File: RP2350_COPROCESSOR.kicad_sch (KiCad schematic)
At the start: 31 parts, among them J2 Conn_01x05, SW6 SW_Push, SW7 SW_Push, U2 RP2350A, U26 W25Q128JVSIQ, Y6 ABM8-272-T3_12MHZ

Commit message: Finished Last sheets
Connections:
- net CAN_STBY: now reaches U2.14 (GPIO10)
- net USBC_CC1_SENSE: now reaches U2.40 (GPIO26/ADC0)
- net USBC_CC2_SENSE: now reaches U2.41 (GPIO27/ADC1)
- net LF_COIL_A renamed LF_TXCT
- net LF_COIL_B renamed LF_COIL_SEL
- net LF_DEMOD renamed LF_SCIO
- no-connect marks 11 -> 8
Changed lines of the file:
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@@
-	)
-	(no_connect
-		(at 157.48 87.63)
 	)
 	(no_connect
@@
 	)
 	(no_connect
-		(at 157.48 130.81)
-	)
-	(no_connect
 		(at 157.48 90.17)
 	)
@@
 	)
 	(no_connect
-		(at 157.48 133.35)
-	)
-	(no_connect
 		(at 157.48 135.89)
 	)
@@
 	(wire
 		(pts
+			(xy 157.48 133.35) (xy 163.83 133.35)
+		)
+		(stroke
+			(width 0)
+			(type default)
+		)
+	)
+	(wire
+		(pts
 			(xy 93.98 125.73) (xy 106.68 125.73)
 		)
@@
 	(wire
 		(pts
+			(xy 157.48 130.81) (xy 163.83 130.81)
+		)
+		(stroke
+			(width 0)
+			(type default)
+		)
+	)
+	(wire
+		(pts
 			(xy 246.38 59.69) (xy 257.81 59.69)
 		)
@@
 		(pts
 			(xy 168.91 48.26) (xy 168.91 49.53)
+		)
+		(stroke
+			(width 0)
+			(type default)
+		)
+	)
+	(wire
+		(pts
+			(xy 157.48 87.63) (xy 163.83 87.63)
 		)
 		(stroke
@@
 		)
 	)
+	(hierarchical_label "USBC_CC1_SENSE"
+		(shape input)
+		(at 163.83 130.81 0)
+		(effects
+			(font
+				(size 1.27 1.27)
+			)
+			(justify left)
+		)
+	)
 	(hierarchical_label "CC1101_C_GDO0"
 		(shape input)
@@
 		)
 	)
-	(hierarchical_label "LF_DEMOD"
+	(hierarchical_label "LF_SCIO"
 		(shape input)
 		(at 163.83 118.11 0)
@@
 		)
 	)
-	(hierarchical_label "LF_COIL_B"
+	(hierarchical_label "LF_COIL_SEL"
 		(shape output)
 		(at 163.83 115.57 0)
@@
 		)
 	)
-	(hierarchical_label "LF_COIL_A"
+	(hierarchical_label "LF_TXCT"
 		(shape output)
 		(at 163.83 113.03 0)
@@
 		)
 	)
+	(hierarchical_label "CAN_STBY"
+		(shape output)
+		(at 163.83 87.63 0)
+		(effects
+			(font
+				(size 1.27 1.27)
+			)
+			(justify left)
+		)
+	)
 	(hierarchical_label "CC1101_A_GDO0"
 		(shape input)
@@
 		(effects
 			(font
+				(size 1.27 1.27)
+			)
+			(justify left)
+		)
+	)
+	(hierarchical_label "USBC_CC2_SENSE"
+		(shape input)
+		(at 163.83 133.35 0)
+		(effects
+			(font

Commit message: finished annotation
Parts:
- renumbered C28 to C27, C30 to C28, C27 to C29, C29 to C30, C40 to C31, C25 to C32, C31 to C33, C32 to C34, C33 to C35, C34 to C36, C35 to C37, C36 to C38, C37 to C39, C38 to C40, C39 to C41, R23 to R24, R24 to R25, R29 to R26, R30 to R27, R25 to R28, R28 to R29, R27 to R30, R26 to R31
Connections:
- net NFC_DWL_REQ: now reaches U2.27 (GPIO16)
- net NFC_VEN: now reaches U2.28 (GPIO17)
- no-connect marks 8 -> 6
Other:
- title: (none) -> RP2350 Coprocessor, Flash, Debug and USB Host
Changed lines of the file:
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@@
 	(generator_version "10.0")
 	(paper "A4")
+	(title_block
+		(title "RP2350 Coprocessor, Flash, Debug and USB Host")
+		(rev "A")
+	)
 	(text "+3V3 I/O DECOUPLING"
 		(exclude_from_sim no)
@@
 	)
 	(no_connect
-		(at 157.48 102.87)
-	)
-	(no_connect
 		(at 157.48 69.85)
 	)
@@
 	)
 	(no_connect
-		(at 157.48 105.41)
-	)
-	(no_connect
 		(at 157.48 110.49)
 	)
@@
 	(wire
 		(pts
+			(xy 157.48 105.41) (xy 163.83 105.41)
+		)
+		(stroke
+			(width 0)
+			(type default)
+		)
+	)
+	(wire
+		(pts
 			(xy 240.03 115.57) (xy 240.03 107.95)
 		)
@@
 	(wire
 		(pts
+			(xy 157.48 102.87) (xy 163.83 102.87)
+		)
+		(stroke
+			(width 0)
+			(type default)
+		)
+	)
+	(wire
+		(pts
 			(xy 195.58 48.26) (xy 195.58 49.53)
 		)
@@
 		)
 	)
+	(hierarchical_label "NFC_VEN"
+		(shape output)
+		(at 163.83 105.41 0)
+		(effects
+			(font
+				(size 1.27 1.27)
+			)
+			(justify left)
+		)
+	)
 	(hierarchical_label "NFC_SCK"
 		(shape output)
@@
 		)
 	)
+	(hierarchical_label "NFC_DWL_REQ"
+		(shape output)
+		(at 163.83 102.87 0)
+		(effects
+			(font
+				(size 1.27 1.27)
+			)
+			(justify left)
+		)
+	)
 	(hierarchical_label "CC1101_C_GDO0"
 		(shape input)
@@
 		(dnp no)
 		(fields_autoplaced yes)
-		(property "Reference" "C38"
+		(property "Reference" "C40"
 			(at 274.32 52.0699 0)
 			(show_name no)
@@
 			(project "FOBtool_HW"
 				(path "/4178b7d0-cf29-4cf2-b214-acbbbd97d338/27b7c62f-0663-47bb-bbed-fbdc5a64ed05"
-					(reference "C38")
+					(reference "C40")
 					(unit 1)
 				)
@@
 		(in_pos_files yes)
 		(dnp no)
-		(property "Reference" "R29"
+		(property "Reference" "R26"
 			(at 70.104 77.216 90)
 			(show_name no)
@@
 			(project "FOBtool_HW"
 				(path "/4178b7d0-cf29-4cf2-b214-acbbbd97d338/27b7c62f-0663-47bb-bbed-fbdc5a64ed05"
-					(reference "R29")
+					(reference "R26")
 					(unit 1)
 				)
@@
 		(dnp no)
 		(fields_autoplaced yes)
-		(property "Reference" "C33"
+		(property "Reference" "C35"
 			(at 212.09 52.0699 0)
 			(show_name no)
@@
 			(project "FOBtool_HW"
 				(path "/4178b7d0-cf29-4cf2-b214-acbbbd97d338/27b7c62f-0663-47bb-bbed-fbdc5a64ed05"
-					(reference "C33")
+					(reference "C35")
 					(unit 1)
 				)
@@
 		(in_pos_files yes)
 		(dnp no)
-		(property "Reference" "C40"
+		(property "Reference" "C31"
 			(at 35.814 129.032 90)
 			(show_name no)
@@
 			(project "FOBtool_HW"
 				(path "/4178b7d0-cf29-4cf2-b214-acbbbd97d338/27b7c62f-0663-47bb-bbed-fbdc5a64ed05"
-					(reference "C40")
+					(reference "C31")
 					(unit 1)
 				)
@@
 		(dnp no)
 		(fields_autoplaced yes)
-		(property "Reference" "C27"
+		(property "Reference" "C29"
 			(at 186.69 24.1299 0)
 			(show_name no)
@@
 			(project "FOBtool_HW"
 				(path "/4178b7d0-cf29-4cf2-b214-acbbbd97d338/27b7c62f-0663-47bb-bbed-fbdc5a64ed05"
-					(reference "C27")
+					(reference "C29")
 					(unit 1)
 				)
@@
 		(dnp no)
 		(fields_autoplaced yes)
-		(property "Reference" "C30"
+		(property "Reference" "C28"
 			(at 172.72 24.1299 0)
 			(show_name no)
@@
 			(project "FOBtool_HW"
 				(path "/4178b7d0-cf29-4cf2-b214-acbbbd97d338/27b7c62f-0663-47bb-bbed-fbdc5a64ed05"
-					(reference "C30")
+					(reference "C28")
 					(unit 1)
 				)
@@
 		(dnp no)
 		(fields_autoplaced yes)
-		(property "Reference" "C32"
+		(property "Reference" "C34"
 			(at 199.39 52.0699 0)
 			(show_name no)
@@
 			(project "FOBtool_HW"
 				(path "/4178b7d0-cf29-4cf2-b214-acbbbd97d338/27b7c62f-0663-47bb-bbed-fbdc5a64ed05"
-					(reference "C32")
+					(reference "C34")
 					(unit 1)
 				)
@@
 		(in_pos_files yes)
 		(dnp no)
-		(property "Reference" "C29"
+		(property "Reference" "C30"
 			(at 35.814 118.872 90)
 			(show_name no)
@@
 			(project "FOBtool_HW"
 				(path "/4178b7d0-cf29-4cf2-b214-acbbbd97d338/27b7c62f-0663-47bb-bbed-fbdc5a64ed05"
-					(reference "C29")
+					(reference "C30")
 					(unit 1)
 				)
@@
 		(dnp no)
 		(fields_autoplaced yes)
-		(property "Reference" "R24"
+		(property "Reference" "R25"
 			(at 44.45 68.58 90)
 			(show_name no)
@@
 			(project "FOBtool_HW"
 				(path "/4178b7d0-cf29-4cf2-b214-acbbbd97d338/27b7c62f-0663-47bb-bbed-fbdc5a64ed05"
-					(reference "R24")
+					(reference "R25")
 					(unit 1)
 				)
@@
 		(dnp no)
 		(fields_autoplaced yes)
-		(property "Reference" "C25"
+		(property "Reference" "C32"
 			(at 172.72 52.0699 0)
 			(show_name no)
@@
 			(project "FOBtool_HW"
 				(path "/4178b7d0-cf29-4cf2-b214-acbbbd97d338/27b7c62f-0663-47bb-bbed-fbdc5a64ed05"
-					(reference "C25")
+					(reference "C32")
 					(unit 1)
 				)
@@
 		(dnp no)
 		(fields_autoplaced yes)
-		(property "Reference" "C28"
+		(property "Reference" "C27"
 			(at 157.48 24.1299 0)
 			(show_name no)
@@
 			(project "FOBtool_HW"
 				(path "/4178b7d0-cf29-4cf2-b214-acbbbd97d338/27b7c62f-0663-47bb-bbed-fbdc5a64ed05"
-					(reference "C28")
+					(reference "C27")
 					(unit 1)
 				)
@@
 		(dnp no)
 		(fields_autoplaced yes)
-		(property "Reference" "R28"
+		(property "Reference" "R29"
 			(at 90.17 119.38 90)
 			(show_name no)
@@
 			(project "FOBtool_HW"
 				(path "/4178b7d0-cf29-4cf2-b214-acbbbd97d338/27b7c62f-0663-47bb-bbed-fbdc5a64ed05"
-					(reference "R28")
+					(reference "R29")
 					(unit 1)
 				)
@@
 		(dnp no)
 		(fields_autoplaced yes)
-		(property "Reference" "C34"
+		(property "Reference" "C36"
 			(at 224.79 52.0699 0)
 			(show_name no)
@@
 			(project "FOBtool_HW"
 				(path "/4178b7d0-cf29-4cf2-b214-acbbbd97d338/27b7c62f-0663-47bb-bbed-fbdc5a64ed05"
-					(reference "C34")
+					(reference "C36")
 					(unit 1)
 				)
@@
 		(dnp no)
 		(fields_autoplaced yes)
-		(property "Reference" "C39"
+		(property "Reference" "C41"
 			(at 270.51 106.6799 0)
 			(show_name no)
@@
 			(project "FOBtool_HW"
 				(path "/4178b7d0-cf29-4cf2-b214-acbbbd97d338/27b7c62f-0663-47bb-bbed-fbdc5a64ed05"
-					(reference "C39")
+					(reference "C41")
 					(unit 1)
 				)
@@
 		(in_pos_files yes)
 		(dnp no)
-		(property "Reference" "R30"
+		(property "Reference" "R27"
 			(at 88.646 84.836 90)
 			(show_name no)
@@
 			(project "FOBtool_HW"
 				(path "/4178b7d0-cf29-4cf2-b214-acbbbd97d338/27b7c62f-0663-47bb-bbed-fbdc5a64ed05"
-					(reference "R30")
+					(reference "R27")
 					(unit 1)
 				)
@@
 		(dnp no)
 		(fields_autoplaced yes)
-		(property "Reference" "C35"
+		(property "Reference" "C37"
 			(at 237.49 52.0699 0)
 			(show_name no)
@@
 			(project "FOBtool_HW"
 				(path "/4178b7d0-cf29-4cf2-b214-acbbbd97d338/27b7c62f-0663-47bb-bbed-fbdc5a64ed05"
-					(reference "C35")
+					(reference "C37")
 					(unit 1)
 				)
@@
 		(dnp no)
 		(fields_autoplaced yes)
-		(property "Reference" "C36"
+		(property "Reference" "C38"
 			(at 250.19 52.0699 0)
 			(show_name no)
@@
 			(project "FOBtool_HW"
 				(path "/4178b7d0-cf29-4cf2-b214-acbbbd97d338/27b7c62f-0663-47bb-bbed-fbdc5a64ed05"
-					(reference "C36")
+					(reference "C38")
 					(unit 1)
 				)
@@
 		(dnp no)
 		(fields_autoplaced yes)
-		(property "Reference" "C37"
+		(property "Reference" "C39"
 			(at 261.62 52.0699 0)
 			(show_name no)
@@
 			(project "FOBtool_HW"
 				(path "/4178b7d0-cf29-4cf2-b214-acbbbd97d338/27b7c62f-0663-47bb-bbed-fbdc5a64ed05"
-					(reference "C37")
+					(reference "C39")
 					(unit 1)
 				)
@@
 		(dnp no)
 		(fields_autoplaced yes)
-		(property "Reference" "R23"
+		(property "Reference" "R24"
 			(at 80.01 25.3999 0)
 			(show_name no)
@@
 			(project "FOBtool_HW"
 				(path "/4178b7d0-cf29-4cf2-b214-acbbbd97d338/27b7c62f-0663-47bb-bbed-fbdc5a64ed05"
-					(reference "R23")
+					(reference "R24")
 					(unit 1)
 				)
@@
 		(dnp no)
 		(fields_autoplaced yes)
-		(property "Reference" "R27"
+		(property "Reference" "R30"
 			(at 213.36 121.92 90)
 			(show_name no)
@@
 			(project "FOBtool_HW"
 				(path "/4178b7d0-cf29-4cf2-b214-acbbbd97d338/27b7c62f-0663-47bb-bbed-fbdc5a64ed05"
-					(reference "R27")
+					(reference "R30")
 					(unit 1)
 				)
@@
 		(dnp no)
 		(fields_autoplaced yes)
-		(property "Reference" "R25"
+		(property "Reference" "R28"
 			(at 38.1 88.9 90)
 			(show_name no)
@@
 			(project "FOBtool_HW"
 				(path "/4178b7d0-cf29-4cf2-b214-acbbbd97d338/27b7c62f-0663-47bb-bbed-fbdc5a64ed05"
-					(reference "R25")
+					(reference "R28")
 					(unit 1)
 				)
@@
 		(dnp yes)
 		(fields_autoplaced yes)
-		(property "Reference" "R26"
+		(property "Reference" "R31"
 			(at 242.57 118.1099 0)
 			(show_name no)
@@
 			(project "FOBtool_HW"
 				(path "/4178b7d0-cf29-4cf2-b214-acbbbd97d338/27b7c62f-0663-47bb-bbed-fbdc5a64ed05"
-					(reference "R26")
+					(reference "R31")
 					(unit 1)
 				)
@@
 		(dnp no)
 		(fields_autoplaced yes)
-		(property "Reference" "C31"
+		(property "Reference" "C33"
 			(at 186.69 52.0699 0)
 			(show_name no)
@@
 			(project "FOBtool_HW"
 				(path "/4178b7d0-cf29-4cf2-b214-acbbbd97d338/27b7c62f-0663-47bb-bbed-fbdc5a64ed05"
-					(reference "C31")
+					(reference "C33")
 					(unit 1)
 				)

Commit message: finished ANCHOR_DOCK sheet
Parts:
- C26, C29, C32: footprint (none) -> Capacitor_SMD:C_0603_1608Metric; DISTRIBUTOR_LINK (none) -> https://eu.mouser.com/en/ProductDetail/Murata-Electronics/G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; MANUFACTURER (none) -> Murata; MPN (none) -> GRM188Z71A475KE15D
- C27, C28, C33, C34, C35, C36, C37, C38, C39, C41: footprint (none) -> Capacitor_SMD:C_0402_1005Metric; DISTRIBUTOR_LINK (none) -> https://www.mouser.com/ProductDetail/Murata-Electronics/GRM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; MANUFACTURER (none) -> Murata; MPN (none) -> GRM155R71C104KA88D; Notes (none) -> N/A
- C30, C31: footprint (none) -> Capacitor_SMD:C_0402_1005Metric; DISTRIBUTOR_LINK (none) -> https://www.mouser.com/ProductDetail/Murata-Electronics/GJM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; MANUFACTURER (none) -> Murata; MPN (none) -> GJM1555C1H150JB01D; Notes (none) -> N/A
- C40: footprint (none) -> Capacitor_SMD:C_0805_2012Metric; DISTRIBUTOR_LINK (none) -> https://www.mouser.com/ProductDetail/Murata-Electronics/GRM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; MANUFACTURER (none) -> Murata; MPN (none) -> GRM21BR71A106KE51L; Notes (none) -> Verify effective capacitance under DC bias.
- J2: value Conn_01x05 -> M50-3530542; footprint (none) -> Connector_PinHeader_1.27mm:PinHeader_1x05_P1.27mm_Vertical; DISTRIBUTOR_LINK (none) -> https://eu.mouser.com/en/ProductDetail/Harwin/M50-3530542?q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; MANUFACTURER (none) -> Harwin; MPN (none) -> M50-3530542; Notes (none) -> Rev-A fitted RP2350 SWD connector. Pin 1 SWCLK, pin 2 GND, 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
- L4: DISTRIBUTOR_LINK (none) -> https://www.mouser.com/ProductDetail/ABRACON/AOTA-B201610S3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; MANUFACTURER (none) -> Abracon; MPN (none) -> AOTA-B201610S3R3-101-T; Notes (none) -> Observe marked inductor orientation.
- R24: footprint (none) -> Resistor_SMD:R_0603_1608Metric; DISTRIBUTOR_LINK (none) -> https://www.mouser.com/ProductDetail/YAGEO/RC0603FR-0733RL?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; MANUFACTURER (none) -> Yageo; MPN (none) -> RC0603FR-0733RL; Notes (none) -> N/A
- R25, R28, R29: footprint (none) -> Resistor_SMD:R_0603_1608Metric; DISTRIBUTOR_LINK (none) -> https://www.mouser.com/ProductDetail/Yageo/RC0603FR-071KL?q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; MANUFACTURER (none) -> Yageo; MPN (none) -> RC0603FR-071KL; Notes (none) -> N/A
- R26, R27: footprint (none) -> Resistor_SMD:R_0603_1608Metric; DISTRIBUTOR_LINK (none) -> https://www.mouser.com/ProductDetail/YAGEO/RC0603FR-0727RL?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; MANUFACTURER (none) -> Yageo; MPN (none) -> RC0603FR-0727RL; Notes (none) -> N/A
- R30: footprint (none) -> Resistor_SMD:R_0603_1608Metric; DISTRIBUTOR_LINK (none) -> https://www.mouser.com/ProductDetail/YAGEO/RC0603JR-070RL?q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; MANUFACTURER (none) -> Yageo; MPN (none) -> RC0603JR-070RL; Notes (none) -> N/A
- R31: footprint (none) -> Resistor_SMD:R_0603_1608Metric; DISTRIBUTOR_LINK (none) -> https://www.mouser.com/ProductDetail/YAGEO/RC0603FR-0710KL?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; MANUFACTURER (none) -> Yageo; MPN (none) -> RC0603FR-0710KL; Notes (none) -> Rev-A DNP; optional QSPI_SS pull-up footprint for alternate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
- SW6, SW7: footprint (none) -> Button_Switch_SMD:SW_SPST_PTS810; DISTRIBUTOR_LINK (none) -> https://www.mouser.com/ProductDetail/CK/PTS810SJM250SMTR-LF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; MANUFACTURER (none) -> C&K; MPN (none) -> PTS810SJM250SMTR LFS; Notes (none) -> Exact Rev-A tactile switch selected
- U2: DISTRIBUTOR_LINK (none) -> https://www.mouser.com/ProductDetail/Raspberry-Pi/SC150913-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; MANUFACTURER (none) -> Raspberry Pi; MPN (none) -> SC1509(13)-A4; Notes (none) -> Assembly: RP2350A exposed pad grounded; X-ray.
- U26: DISTRIBUTOR_LINK (none) -> https://www.mouser.com/ProductDetail/Winbond/W25Q128JVSIQ-T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; MANUFACTURER (none) -> Winbond; MPN (none) -> W25Q128JVSIQTR; Notes (none) -> N/A
- Y6: footprint (none) -> Crystal:Crystal_SMD_Abracon_ABM8G-4Pin_3.2x2.5mm; DISTRIBUTOR_LINK (none) -> https://www.mouser.com/ProductDetail/ABRACON/ABM8-272-T3?qs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; MANUFACTURER (none) -> Abracon; MPN (none) -> ABM8-272-T3; Notes (none) -> Ground crystal case pads 2/4.
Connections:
- net USB_HOST_FAULT_N: now also U2.31 (GPIO19); no longer U2.36 (GPIO24)
- net DOCK_SENSE: now reaches U2.15 (GPIO11)
- net DOCK_LINK_B: now reaches U2.37 (GPIO25)
- net DOCK_VBUS_EN: now reaches U2.42 (GPIO28/ADC2)
- net DOCK_FAULT_N: now reaches U2.43 (GPIO29/ADC3)
- net DOCK_SYNC: now reaches U2.5 (GPIO3)
- new net DOCK_LINK_A: U2.36 (GPIO24)
- no-connect marks 6 -> 0

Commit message: the schematic is finished
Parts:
- C26, C29, C32: Notes (none) -> N/A
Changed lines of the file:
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@@
 	)
 	(hierarchical_label "DOCK_LINK_A"
-		(shape input)
+		(shape output)
 		(at 163.83 123.19 0)
 		(effects
@@
 			)
 		)
-		(property "Notes" ""
+		(property "Notes" "N/A"
 			(at 182.88 25.4 0)
 			(hide yes)
@@
 			)
 		)
-		(property "Notes" ""
+		(property "Notes" "N/A"
 			(at 168.91 53.34 0)
 			(hide yes)
@@
 			)
 		)
-		(property "Notes" ""
+		(property "Notes" "N/A"
 			(at 77.47 44.45 0)
 			(hide yes)

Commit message: finished schematic phase
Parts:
- L4: footprint (none) -> FOBtool_Custom:L_Abracon_AOTA-B201610S_2.0x1.6mm
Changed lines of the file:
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@@
 			)
 		)
-		(property "Footprint" ""
+		(property "Footprint" "FOBtool_Custom:L_Abracon_AOTA-B201610S_2.0x1.6mm"
 			(at 137.16 34.29 0)
 			(hide yes)

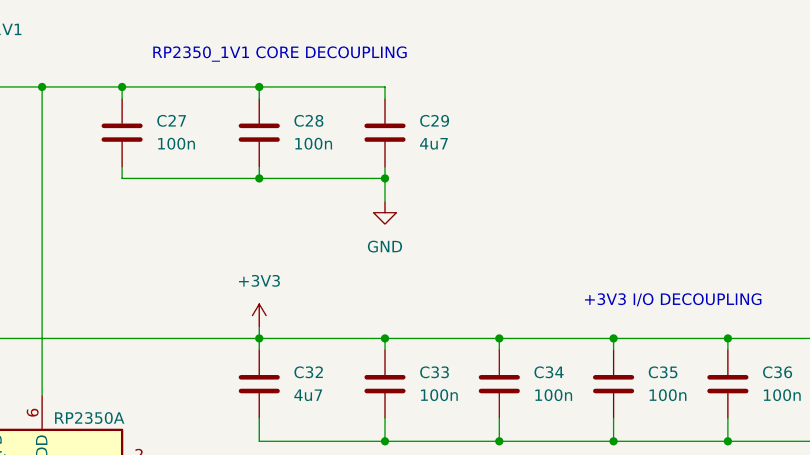
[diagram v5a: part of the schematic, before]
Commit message: finished initial placement for rp2350A and esp32
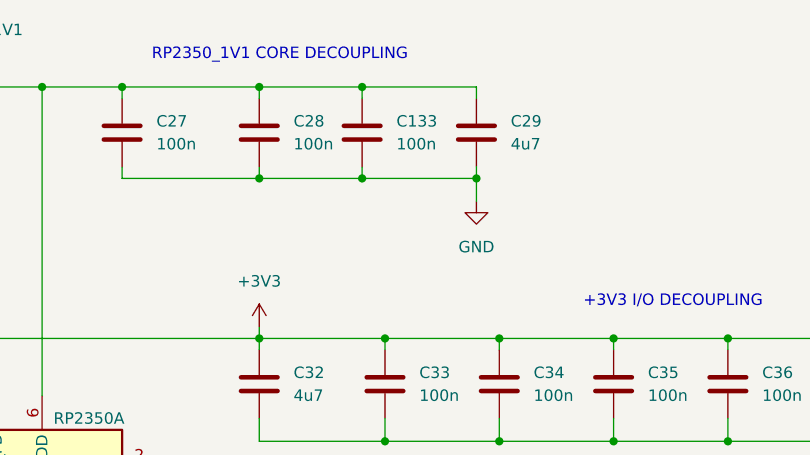
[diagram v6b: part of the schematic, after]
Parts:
- added C133: 100n, Capacitor_SMD:C_0402_1005Metric, symbol Device:C
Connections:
- net GND: now also C133.2
- net RP2350_1V1: now also C133.1
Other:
- moved on the sheet: C29
